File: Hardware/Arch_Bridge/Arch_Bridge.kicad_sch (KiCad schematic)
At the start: 95 parts, among them J1 Conn_01x02, J3 Conn_01x04, J4 Conn_01x04, Q1 2N3904, Q2 MJE2955, Q3 MJE2955, U1 AP63205WU, U11 ESP32-S3-WROOM-1, U12 TXS0102DCT, U13 DRV8231ADDAR, U17 TXS0102DCT, U18 TXS0102DCT, U19 TXS0108EPW, U2 TLV1117LV33DCYR, U20 TXS0108EPW, U3 LM393B, U4 74LVC1G04, U5 74LVC1G02, U6 TLP2770, U7 DRV8231ADDAR

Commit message: Checkpoint
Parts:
- removed F3: 250mA, Fuse:Fuse_1206_3216Metric, symbol Device:Polyfuse
- added D10: Z-12, Diode_SMD:D_MiniMELF, symbol Device:D_Zener
- D3, D5: value 1N5231B -> Z-5.1; footprint Diode_THT:D_DO-35_SOD27_P7.62mm_Horizontal -> Diode_SMD:D_MiniMELF; LCSC SKU C895239 -> C550442; MFG Onsemi -> Nexperia; PN 1N5231B -> BZV55-C5V1,135
- Q1: value 2N3904 -> MMBT3904; footprint Package_TO_SOT_THT:TO-92_Inline -> Package_TO_SOT_SMD:SOT-23; symbol Transistor_BJT:2N3904 -> Transistor_BJT:MMBT3904; LCSC SKU C2980867 -> C77991; MFG Diotec Semiconductor -> MCC; PN 2N3904 -> MMBT3904-TP
- Q2: value MJE2955 -> MMBT3906; footprint Package_TO_SOT_THT:TO-220-3_Vertical -> Package_TO_SOT_SMD:SOT-23; symbol Transistor_BJT:TIP2955 -> Transistor_BJT:MMBT3906; LCSC SKU C184196 -> C77990; MFG Onsemi -> MCC; PN MJE2955TG -> MMBT3906
- R9: footprint Resistor_THT:R_Axial_DIN0414_L11.9mm_D4.5mm_P7.62mm_Vertical -> Resistor_THT:R_Axial_DIN0516_L15.5mm_D5.0mm_P5.08mm_Vertical
- V12: renamed from V12A1; now fitted; now in the parts list
- V12A1: renamed from V12; now not fitted; now left out of the parts list
- renumbered F2 to F1, F4 to F2
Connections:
- net +12V: now also R14.2
- net GND: now also Q1.2 (E), D10.2 (A); no longer Q1.1 (E)
- net at R2.1: now also Q1.1 (B); no longer Q1.2 (B)
- net at Q2.2 (E): now also JP1.1, D10.1 (K); no longer R10.2
- net at Q2.3 (C): now also R10.2; no longer JP1.1
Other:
- moved on the sheet: JP1

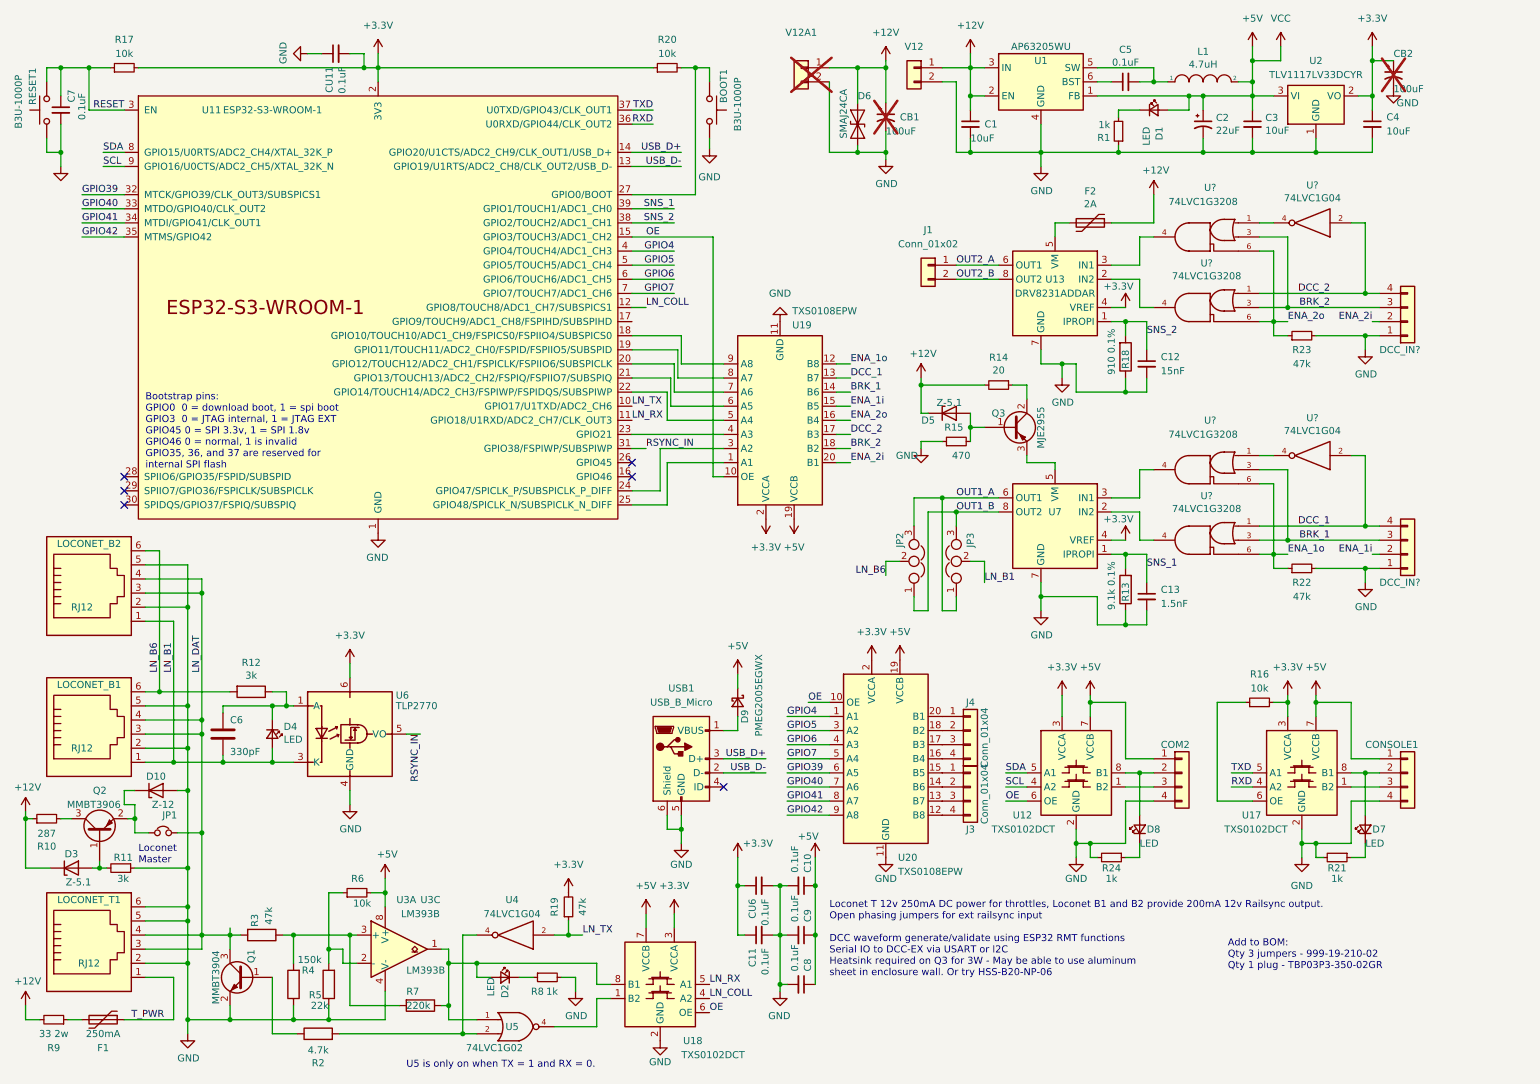
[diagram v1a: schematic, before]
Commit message: Revised PCB to fix thermal problems, improve usage of board space. DCC inputs, serial ports, and GPIO all have independent IOREF connections.
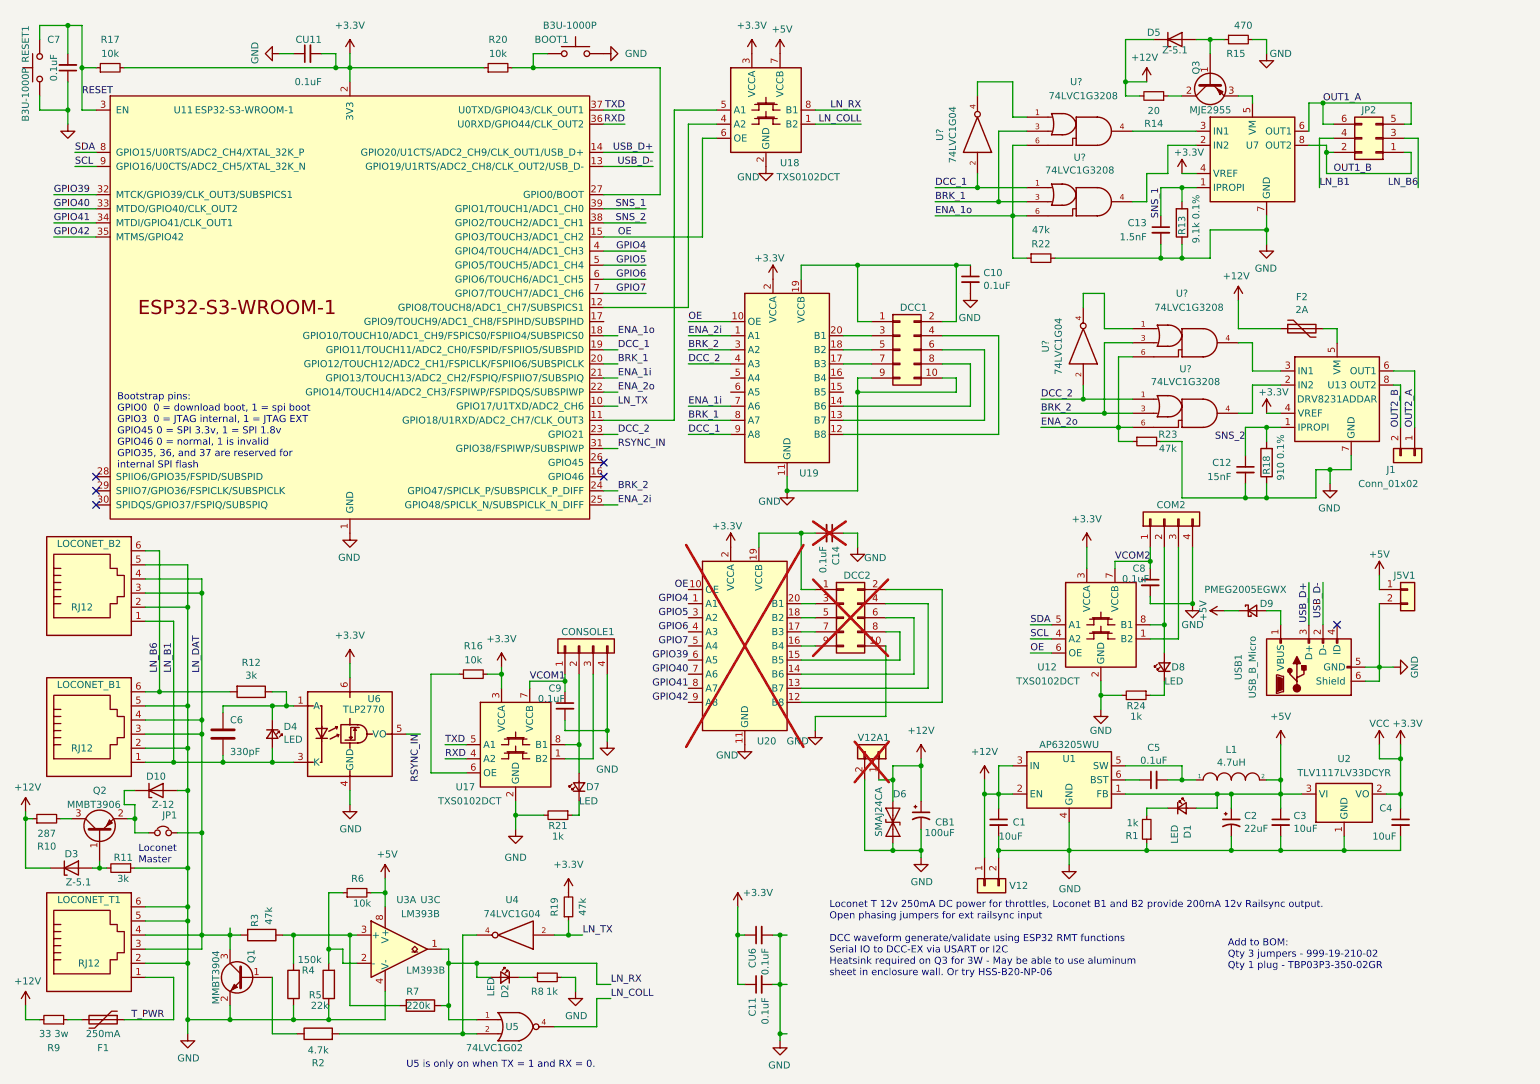
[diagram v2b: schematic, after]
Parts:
- removed CB2: 100uF, Capacitor_THT:CP_Radial_D8.0mm_P3.50mm, symbol Device:C_Polarized_Small_US
- removed DCC_IN? (x2): Conn_01x04_Female, Connector_PinSocket_2.54mm:PinSocket_1x04_P2.54mm_Vertical, symbol Connector_Generic:Conn_01x04
- removed J3, J4: Conn_01x04, Connector_PinSocket_2.54mm:PinSocket_1x04_P2.54mm_Vertical, symbol Connector_Generic:Conn_01x04
- removed JP2, JP3: Jumper_NC_Dual, Connector_PinHeader_2.54mm:PinHeader_1x03_P2.54mm_Vertical, symbol Loconet DCC Interface ESP32-rescue:Jumper_NC_Dual-Device
- added C14: 0.1uF, Capacitor_SMD:C_1206_3216Metric, symbol Device:C_Small
- added DCC1, DCC2: Conn_02x05_Odd_Even, Connector_PinSocket_2.54mm:PinSocket_2x05_P2.54mm_Vertical, symbol Connector_Generic:Conn_02x05_Odd_Even
- added J5V1: Conn_01x02, Connector_PinSocket_2.54mm:PinSocket_1x02_P2.54mm_Vertical, symbol Connector_Generic:Conn_01x02
- added JP2: Conn_02x03_Odd_Even, Connector_PinSocket_2.54mm:PinSocket_2x03_P2.54mm_Vertical, symbol Connector_Generic:Conn_02x03_Odd_Even
- C1, C3, C4: LCSC SKU C96600 -> C380537; PN CL31A106MBHNNNE -> CL32A106KBJNNNE
- CB1: footprint Capacitor_THT:CP_Radial_D8.0mm_P3.50mm -> Capacitor_SMD:CP_Elec_8x10; LCSC SKU (none) -> C696384; MFG Wuerth Electronik -> Kemet; PN 860010674014 -> EDK107M050A9MAA; now fitted; now in the parts list
- COM2: LCSC SKU (none) -> C3323964; MFG 3M -> Samtec; PN 929850-01-04-RA -> SSW-104-01-T-S
- CONSOLE1: value Conn_01x03 -> Conn_01x04; LCSC SKU (none) -> C3323964; MFG 3M -> Samtec; PN 929850-01-04-RA -> SSW-104-01-T-S
- R9: value 33 2w -> 33 3w; LCSC SKU C601882 -> C1761032; MFG C601882 -> YAEGO; PN FMP200JTF52-33R -> FMP300FRF73-33R
- U20: now not fitted; now left out of the parts list
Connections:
- net +3.3V: now also U?.5 (VCC), U?.5 (VCC), U?.5 (VCC), U?.5 (VCC), U?.5 (VCC), U?.5 (VCC)
- net +5V: now also J5V1.1 (Pin_1); no longer C10.1, C8.1, C9.1, COM2.1 (Pin_1), CONSOLE1.1 (Pin_1), U12.7 (VCCB), U17.7 (VCCB), U19.19 (VCCB), U20.19 (VCCB), U?.5 (VCC), U?.5 (VCC), U?.5 (VCC), U?.5 (VCC), U?.5 (VCC), U?.5 (VCC)
- net BRK_1: now also U11.20 (GPIO12/TOUCH12/ADC2_CH1/FSPICLK/FSPIIO6/SUBSPICLK), U19.8 (A7); no longer U19.14 (B6)
- net BRK_2: now also U11.24 (GPIO47/SPICLK_P/SUBSPICLK_P_DIFF), U19.3 (A2); no longer U19.18 (B2)
- net DCC_1: now also U11.19 (GPIO11/TOUCH11/ADC2_CH0/FSPID/FSPIIO5/SUBSPID), U19.9 (A8); no longer U19.13 (B7)
- net DCC_2: now also U11.23 (GPIO21), U19.4 (A3); no longer U19.17 (B3)
- net ENA_1i: now also U11.21 (GPIO13/TOUCH13/ADC2_CH2/FSPIQ/FSPIIO7/SUBSPIQ), U19.7 (A6); no longer U19.15 (B5)
- net ENA_1o: now also U11.18 (GPIO10/TOUCH10/ADC1_CH9/FSPICS0/FSPIIO4/SUBSPICS0); no longer U19.12 (B8)
- net ENA_2i: now also U11.25 (GPIO48/SPICLK_N/SUBSPICLK_N_DIFF), U19.1 (A1); no longer U19.20 (B1)
- net ENA_2o: now also U11.22 (GPIO14/TOUCH14/ADC2_CH3/FSPIWP/FSPIDQS/SUBSPIWP); no longer U19.16 (B4)
- net GND: now also C7.1, R15.2, C14.1, DCC1.10 (Pin_10), DCC1.9 (Pin_9), DCC2.10 (Pin_10), J5V1.2 (Pin_2); no longer C7.2, R15.1
- net LN_B1: now also JP2.4 (Pin_4)
- net LN_B6: now also JP2.3 (Pin_3)
- net LN_COLL: now also U18.1 (B2), U5.4; no longer U11.12 (GPIO8/TOUCH8/ADC1_CH7/SUBSPICS1), U18.4 (A2)
- net LN_RX: now also D2.2 (A), R7.1, U18.8 (B1), U3.1, U5.1; no longer U11.11 (GPIO18/U1RXD/ADC2_CH7/CLK_OUT3), U18.5 (A1)
- net OUT1_A: now also JP2.5 (Pin_5), JP2.6 (Pin_6)
- net OUT1_B: now also JP2.1 (Pin_1), JP2.2 (Pin_2)
- net RESET: now also C7.2; no longer C7.1
- net at D5.2 (A), Q3.1 (B): now also R15.1; no longer R15.2
- net at U19.6 (A5): no longer U11.21 (GPIO13/TOUCH13/ADC2_CH2/FSPIQ/FSPIIO7/SUBSPIQ)
- net at U19.5 (A4): no longer U11.22 (GPIO14/TOUCH14/ADC2_CH3/FSPIWP/FSPIDQS/SUBSPIWP)
- net at U20.12 (B8): now also DCC2.2 (Pin_2)
- net at U20.13 (B7): now also DCC2.4 (Pin_4)
- net at U20.14 (B6): now also DCC2.6 (Pin_6)
- net at U20.15 (B5): now also DCC2.8 (Pin_8)
- net at U20.16 (B4): now also DCC2.9 (Pin_9)
- net at U20.17 (B3): now also DCC2.7 (Pin_7)
- net at U20.18 (B2): now also DCC2.5 (Pin_5)
- net at U20.20 (B1): now also DCC2.3 (Pin_3)
- new net: U11.11 (GPIO18/U1RXD/ADC2_CH7/CLK_OUT3), U18.5 (A1)
- new net: U11.12 (GPIO8/TOUCH8/ADC1_CH7/SUBSPICS1), U18.4 (A2)
- new net: C14.2, DCC2.1 (Pin_1), U20.19 (VCCB)
- new net: C10.1, DCC1.1 (Pin_1), DCC1.2 (Pin_2), U19.19 (VCCB)
- new net: DCC1.4 (Pin_4), U19.12 (B8)
- new net: DCC1.6 (Pin_6), U19.13 (B7)
- new net: DCC1.8 (Pin_8), U19.14 (B6)
- new net: DCC1.7 (Pin_7), U19.17 (B3)
- new net: DCC1.5 (Pin_5), U19.18 (B2)
- new net: DCC1.3 (Pin_3), U19.20 (B1)
- new net VCOM1: C9.1, CONSOLE1.1 (Pin_1), U17.7 (VCCB)
- new net VCOM2: C8.1, COM2.1 (Pin_1), U12.7 (VCCB)
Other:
- moved on the sheet: BOOT1, C1, C10, C11, C12, C13, C2, C3, C4, C5, C7, C8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

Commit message: Board revision progress
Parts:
- added R25: 10k, Resistor_SMD:R_1206_3216Metric, symbol Device:R_Small
- D10: value Z-12 -> Z-13; LCSC SKU C426807 -> C550391; PN BZV55-B12,115 -> BZV55-B13,115
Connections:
- net GND: now also R25.2
- net OE: now also R25.1
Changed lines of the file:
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@@
   (junction (at 208.915 135.89) (diameter 0) (color 0 0 0 0)
   )
+  (junction (at 148.59 41.91) (diameter 0) (color 0 0 0 0)
+  )
   (junction (at 103.505 157.48) (diameter 0) (color 0 0 0 0)
   )
@@
   (junction (at 59.69 147.955) (diameter 0) (color 0 0 0 0)
   )
+  (junction (at 137.16 41.91) (diameter 0) (color 0 0 0 0)
+  )
   (junction (at 100.965 132.08) (diameter 0) (color 0 0 0 0)
   )
@@
     (stroke (width 0) (type default))
   )
+  (wire (pts (xy 148.59 41.91) (xy 148.59 43.18))
+    (stroke (width 0) (type default))
+  )
   (wire (pts (xy 190.5 161.29) (xy 190.5 163.83))
     (stroke (width 0) (type default))
@@
     (stroke (width 0) (type default))
   )
+  (wire (pts (xy 148.59 41.91) (xy 148.59 40.64))
+    (stroke (width 0) (type default))
+  )
   (wire (pts (xy 119.38 60.96) (xy 127 60.96))
     (stroke (width 0) (type default))
@@
     (stroke (width 0) (type default))
   )
-  (wire (pts (xy 137.16 53.34) (xy 137.16 35.56))
+  (wire (pts (xy 137.16 53.34) (xy 137.16 41.91))
     (stroke (width 0) (type default))
   )
@@
     (stroke (width 0) (type default))
   )
+  (wire (pts (xy 144.78 41.91) (xy 148.59 41.91))
+    (stroke (width 0) (type default))
+  )
   (wire (pts (xy 171.45 148.59) (xy 176.53 148.59))
     (stroke (width 0) (type default))
@@
     (stroke (width 0) (type default))
   )
+  (wire (pts (xy 137.16 41.91) (xy 139.7 41.91))
+    (stroke (width 0) (type default))
+  )
   (wire (pts (xy 186.69 41.91) (xy 186.69 44.45))
     (stroke (width 0) (type default))
@@
     (stroke (width 0) (type default))
   )
+  (wire (pts (xy 137.16 41.91) (xy 137.16 35.56))
+    (stroke (width 0) (type default))
+  )
   (wire (pts (xy 213.36 17.78) (xy 218.44 17.78))
     (stroke (width 0) (type default))
@@
       (effects (font (size 1.27 1.27)))
     )
-    (property "Value" "Z-12" (at 40.005 155.575 0)
+    (property "Value" "Z-13" (at 40.005 155.575 0)
       (effects (font (size 1.27 1.27)))
     )
@@
       (effects (font (size 1.27 1.27)) hide)
     )
-    (property "PN" "BZV55-B12,115" (at 38.735 153.035 0)
+    (property "PN" "BZV55-B13,115" (at 38.735 153.035 0)
       (effects (font (size 1.27 1.27)) hide)
     )
-    (property "LCSC SKU" "C426807" (at 38.735 153.035 0)
+    (property "LCSC SKU" "C550391" (at 38.735 153.035 0)
       (effects (font (size 1.27 1.27)) hide)
     )
@@
     )
   )
+  (symbol (lib_id "Device:R_Small") (at 142.24 41.91 90) (unit 1)
+    (in_bom yes) (on_board yes) (dnp no)
+    (property "Reference" "R25" (at 142.24 43.815 90)
+      (effects (font (size 1.27 1.27)))
+    )
+    (property "Value" "10k" (at 142.24 45.72 90)
+      (effects (font (size 1.27 1.27)))
+    )
+    (property "Footprint" "Resistor_SMD:R_1206_3216Metric" (at 142.24 41.91 0)
+      (effects (font (size 1.27 1.27)) hide)
+    )
+    (property "Datasheet" "https://www.mouser.com/datasheet/2/54/cr-1858361.pdf" (at 142.24 41.91 0)
+      (effects (font (size 1.27 1.27)) hide)
+    )
+    (property "MFG" "YAEGO" (at 142.24 41.91 0)
+      (effects (font (size 1.27 1.27)) hide)
+    )
+    (property "PN" "RC1206FR-1310KL" (at 142.24 41.91 0)
+      (effects (font (size 1.27 1.27)) hide)
+    )
+    (property "LCSC SKU" "C4303232" (at 142.24 41.91 0)
+      (effects (font (size 1.27 1.27)) hide)
+    )
+    (pin "1")
+    (pin "2")
+    (instances
+      (project "Arch_Bridge"
+        (path "/56f7722c-599e-4f4b-8e1a-4387b51291ab"
+          (reference "R25") (unit 1)
+        )
+      )
+      (project "Booster 4ch ESP32"
+        (path "/ca466827-dc9b-41a9-af5b-af8cb0cad0b9"
+          (reference "R?") (unit 1)
+        )
+      )
+    )
+  )
   (symbol (lib_id "Device:C_Small") (at 234.95 95.25 0) (mirror y) (unit 1)
     (in_bom yes) (on_board yes) (dnp no) (fields_autoplaced)
@@
     )
   )
-  (symbol (lib_id "power:GND") (at 148.59 40.64 0) (unit 1)
+  (symbol (lib_id "power:GND") (at 148.59 43.18 0) (unit 1)
     (in_bom yes) (on_board yes) (dnp no)
-    (property "Reference" "#PWR020" (at 148.59 46.99 0)
+    (property "Reference" "#PWR020" (at 148.59 49.53 0)
       (effects (font (size 1.27 1.27)) hide)
     )
-    (property "Value" "GND" (at 145.415 42.545 0)
+    (property "Value" "GND" (at 151.765 45.72 0)
       (effects (font (size 1.27 1.27)))
     )
-    (property "Footprint" "" (at 148.59 40.64 0)
+    (property "Footprint" "" (at 148.59 43.18 0)
       (effects (font (size 1.27 1.27)) hide)
     )
-    (property "Datasheet" "" (at 148.59 40.64 0)
+    (property "Datasheet" "" (at 148.59 43.18 0)
       (effects (font (size 1.27 1.27)) hide)
     )
